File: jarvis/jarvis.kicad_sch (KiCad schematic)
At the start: 37 parts, among them IC1 ESP32-S3R16V, IC2 MAX98357AETE+T, IC3 MCP73871T-4CAI_ML, IC4 TLV70033DDCT, J1 Conn_01x02 - Speaker, J2 Mic Conn_01x05, J3 Conn_01x02 - Battery, U1 W25Q64JVSSIQ, U2 2137160001, Y1 Crystal 32.768khz, Y2 Crystal 40mhz

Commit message: flash routed
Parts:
- removed C1, C4, C5: 1uf, Capacitor_SMD:C_0603_1608Metric, symbol Device:C
- removed C10, C7, C8, C9: 12pf, Capacitor_SMD:C_0402_1005Metric, symbol Device:C
- removed C11, C12, C13, C14, C15, C16, C17: 0.1uf, Capacitor_SMD:C_0603_1608Metric, symbol Device:C
- removed C2, C6: 10uf, Capacitor_SMD:C_0603_1608Metric, symbol Device:C
- removed C3: 4.7uf, Capacitor_SMD:C_0603_1608Metric, symbol Device:C
- removed IC1: ESP32-S3R16V, jarvis:esp32-s3r16v, symbol jarvis:ESP32-S3R16V
- removed IC2: MAX98357AETE+T, jarvis:LIB_MAX98357AETE+T, symbol jarvis:MAX98357AETE+T
- removed IC3: MCP73871T-4CAI_ML, jarvis:MCP73871T-4CAI ML, symbol jarvis:MCP73871T-4CAI_ML
- removed IC4: TLV70033DDCT, jarvis:TLV70033DDCT, symbol jarvis:TLV70033DDCT
- removed J1: Conn_01x02 - Speaker, Connector_Molex:Molex_PicoBlade_53047-0210_1x02_P1.25mm_Vertical, symbol Connector_Generic:Conn_01x02
- removed J2: Mic Conn_01x05, Connector_Molex:Molex_PicoBlade_53047-0510_1x05_P1.25mm_Vertical, symbol Connector_Generic:Conn_01x05
- removed J3: Conn_01x02 - Battery, Connector_Molex:Molex_PicoBlade_53047-0210_1x02_P1.25mm_Vertical, symbol Connector_Generic:Conn_01x02
- removed L1: 24nh, jarvis:MLG1005SR24JT000, symbol jarvis:MLG1005SR24JT000
- removed PESD5: PESD5V0X1UAB,115, jarvis:PESD5V0X1UAB115, symbol jarvis:PESD5V0X1UAB,115
- removed R1: 2k, Resistor_SMD:R_0603_1608Metric, symbol Device:R
- removed R2: 10k, Resistor_SMD:R_0603_1608Metric, symbol Device:R
- removed R3, R4: 5.1k, Resistor_SMD:R_0603_1608Metric, symbol Device:R
- removed R5, R6: 22, Resistor_SMD:R_0603_1608Metric, symbol Device:R
- removed R7: 5M, Resistor_SMD:R_0603_1608Metric, symbol Device:R
- removed U1: W25Q64JVSSIQ, jarvis:W25Q64JVSSIQ, symbol jarvis:W25Q64JVSSIQ
- removed U2: 2137160001, jarvis:2137160001_MOL, symbol jarvis:2137160001
- removed Y1: Crystal 32.768khz, jarvis:XTAL_CM8V-T1A-32.768KHZ-7PF-20PPM-TA-QC, symbol jarvis:CM8V-T1A-32.768KHZ-7PF-20PPM-TA-QC
- removed Y2: Crystal 40mhz, jarvis:XTAL_CM8V-T1A-32.768KHZ-7PF-20PPM-TA-QC, symbol jarvis:CM8V-T1A-32.768KHZ-7PF-20PPM-TA-QC
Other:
- added sheet Components (components.kicad_sch)
- added sheet ESP (esp.kicad_sch)
- added sheet Power (untitled.kicad_sch)

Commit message: initial all connections
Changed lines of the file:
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@@
 			)
 		)
-		(pin "USB-DP" input
+		(pin "USB-DP" output
 			(at 213.36 52.07 180)
 			(effects

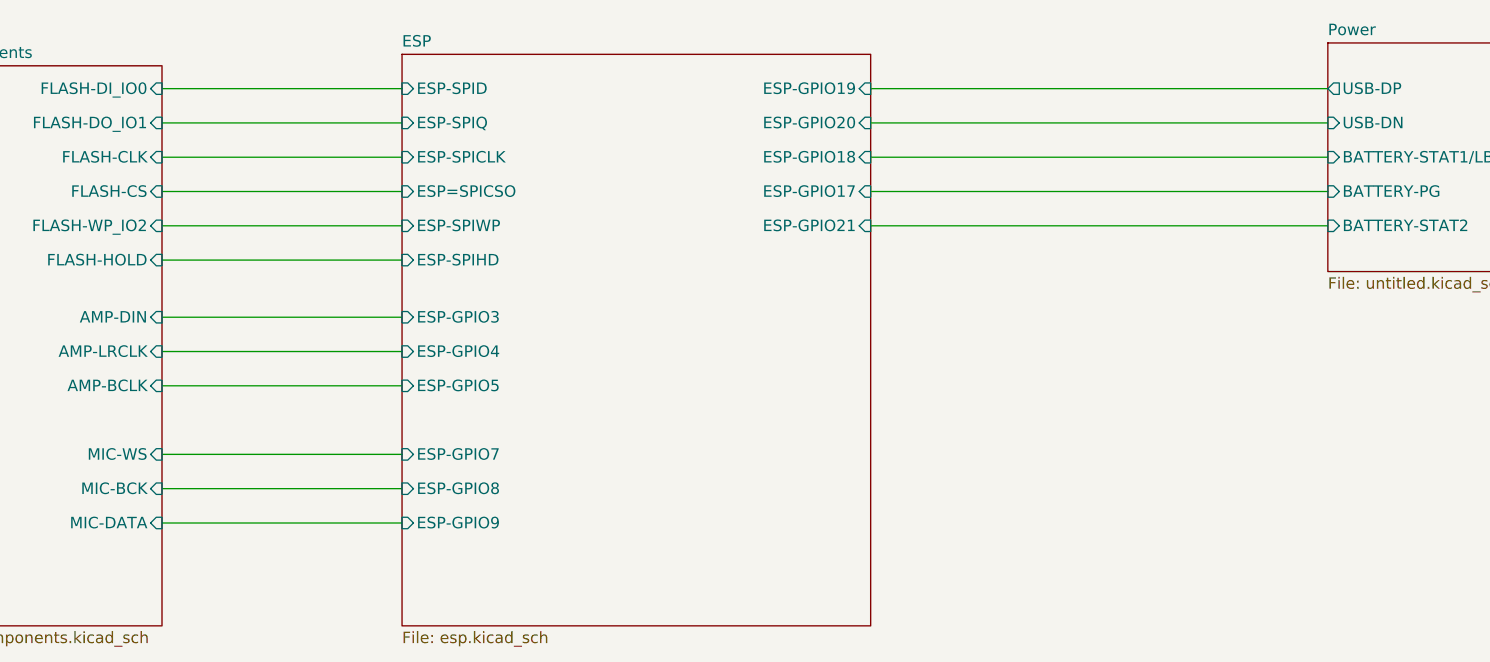
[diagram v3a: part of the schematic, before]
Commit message: with leds and boot button
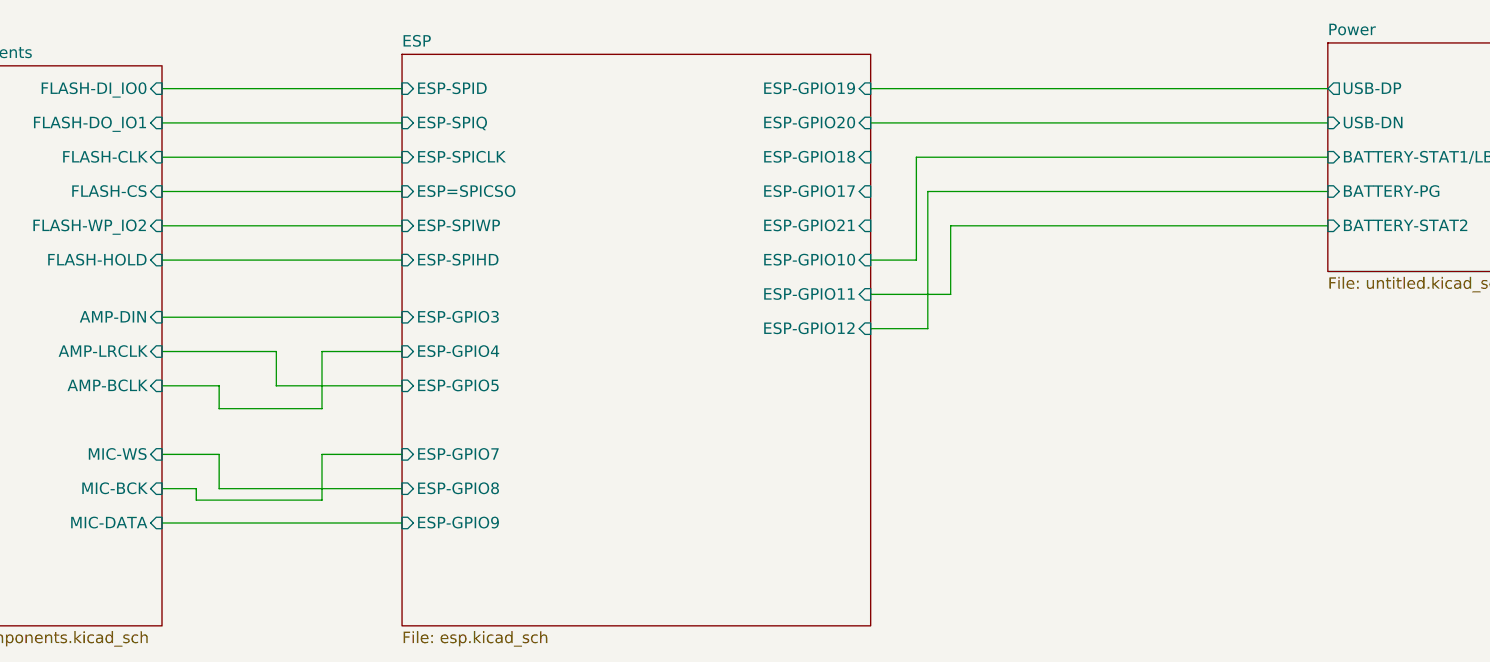
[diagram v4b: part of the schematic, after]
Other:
- sheet ESP ports: added ESP-GPIO10, ESP-GPIO11, ESP-GPIO12; removed none
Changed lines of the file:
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@@
 	(wire
 		(pts
-			(xy 83.82 81.28) (xy 110.49 81.28)
+			(xy 96.52 85.09) (xy 110.49 85.09)
 		)
 		(stroke
@@
 	(wire
 		(pts
+			(xy 87.63 97.79) (xy 87.63 96.52)
+		)
+		(stroke
+			(width 0)
+			(type default)
+		)
+	)
+	(wire
+		(pts
+			(xy 171.45 67.31) (xy 171.45 74.93)
+		)
+		(stroke
+			(width 0)
+			(type default)
+		)
+	)
+	(wire
+		(pts
 			(xy 83.82 100.33) (xy 110.49 100.33)
 		)
@@
 	(wire
 		(pts
-			(xy 83.82 96.52) (xy 110.49 96.52)
-		)
-		(stroke
-			(width 0)
-			(type default)
-		)
-	)
-	(wire
-		(pts
 			(xy 83.82 63.5) (xy 110.49 63.5)
 		)
@@
 	(wire
 		(pts
-			(xy 162.56 67.31) (xy 213.36 67.31)
+			(xy 171.45 74.93) (xy 162.56 74.93)
+		)
+		(stroke
+			(width 0)
+			(type default)
+		)
+	)
+	(wire
+		(pts
+			(xy 83.82 92.71) (xy 90.17 92.71)
+		)
+		(stroke
+			(width 0)
+			(type default)
+		)
+	)
+	(wire
+		(pts
+			(xy 168.91 63.5) (xy 213.36 63.5)
+		)
+		(stroke
+			(width 0)
+			(type default)
+		)
+	)
+	(wire
+		(pts
+			(xy 90.17 87.63) (xy 90.17 85.09)
+		)
+		(stroke
+			(width 0)
+			(type default)
+		)
+	)
+	(wire
+		(pts
+			(xy 87.63 96.52) (xy 83.82 96.52)
+		)
+		(stroke
+			(width 0)
+			(type default)
+		)
+	)
+	(wire
+		(pts
+			(xy 110.49 81.28) (xy 101.6 81.28)
+		)
+		(stroke
+			(width 0)
+			(type default)
+		)
+	)
+	(wire
+		(pts
+			(xy 96.52 81.28) (xy 96.52 85.09)
+		)
+		(stroke
+			(width 0)
+			(type default)
+		)
+	)
+	(wire
+		(pts
+			(xy 168.91 63.5) (xy 168.91 78.74)
 		)
 		(stroke
@@
 	(wire
 		(pts
-			(xy 83.82 85.09) (xy 110.49 85.09)
-		)
-		(stroke
-			(width 0)
-			(type default)
-		)
-	)
-	(wire
-		(pts
-			(xy 213.36 59.69) (xy 162.56 59.69)
+			(xy 83.82 81.28) (xy 96.52 81.28)
+		)
+		(stroke
+			(width 0)
+			(type default)
+		)
+	)
+	(wire
+		(pts
+			(xy 101.6 92.71) (xy 101.6 97.79)
+		)
+		(stroke
+			(width 0)
+			(type default)
+		)
+	)
+	(wire
+		(pts
+			(xy 167.64 71.12) (xy 167.64 59.69)
+		)
+		(stroke
+			(width 0)
+			(type default)
+		)
+	)
+	(wire
+		(pts
+			(xy 90.17 96.52) (xy 110.49 96.52)
+		)
+		(stroke
+			(width 0)
+			(type default)
+		)
+	)
+	(wire
+		(pts
+			(xy 101.6 97.79) (xy 87.63 97.79)
+		)
+		(stroke
+			(width 0)
+			(type default)
+		)
+	)
+	(wire
+		(pts
+			(xy 167.64 71.12) (xy 162.56 71.12)
+		)
+		(stroke
+			(width 0)
+			(type default)
+		)
+	)
+	(wire
+		(pts
+			(xy 90.17 92.71) (xy 90.17 96.52)
+		)
+		(stroke
+			(width 0)
+			(type default)
+		)
+	)
+	(wire
+		(pts
+			(xy 213.36 67.31) (xy 171.45 67.31)
+		)
+		(stroke
+			(width 0)
+			(type default)
+		)
+	)
+	(wire
+		(pts
+			(xy 83.82 85.09) (xy 90.17 85.09)
+		)
+		(stroke
+			(width 0)
+			(type default)
+		)
+	)
+	(wire
+		(pts
+			(xy 110.49 92.71) (xy 101.6 92.71)
+		)
+		(stroke
+			(width 0)
+			(type default)
+		)
+	)
+	(wire
+		(pts
+			(xy 101.6 87.63) (xy 90.17 87.63)
 		)
 		(stroke
@@
 	(wire
 		(pts
+			(xy 101.6 81.28) (xy 101.6 87.63)
+		)
+		(stroke
+			(width 0)
+			(type default)
+		)
+	)
+	(wire
+		(pts
+			(xy 167.64 59.69) (xy 213.36 59.69)
+		)
+		(stroke
+			(width 0)
+			(type default)
+		)
+	)
+	(wire
+		(pts
 			(xy 83.82 55.88) (xy 110.49 55.88)
 		)
@@
 	(wire
 		(pts
-			(xy 162.56 63.5) (xy 213.36 63.5)
+			(xy 162.56 78.74) (xy 168.91 78.74)
 		)
 		(stroke
@@
 		(pts
 			(xy 83.82 67.31) (xy 110.49 67.31)
-		)
-		(stroke
-			(width 0)
-			(type default)
-		)
-	)
-	(wire
-		(pts
-			(xy 83.82 92.71) (xy 110.49 92.71)
 		)
 		(stroke
@@
 			)
 		)
+		(pin "ESP-GPIO10" input
+			(at 162.56 71.12 0)
+			(effects
+				(font
+					(size 1.27 1.27)
+				)
+				(justify right)
+			)
+		)
+		(pin "ESP-GPIO11" input
+			(at 162.56 74.93 0)
+			(effects
+				(font
+					(size 1.27 1.27)
+				)
+				(justify right)
+			)
+		)
+		(pin "ESP-GPIO12" input
+			(at 162.56 78.74 0)
+			(effects
+				(font
+					(size 1.27 1.27)
+				)
+				(justify right)
+			)
+		)

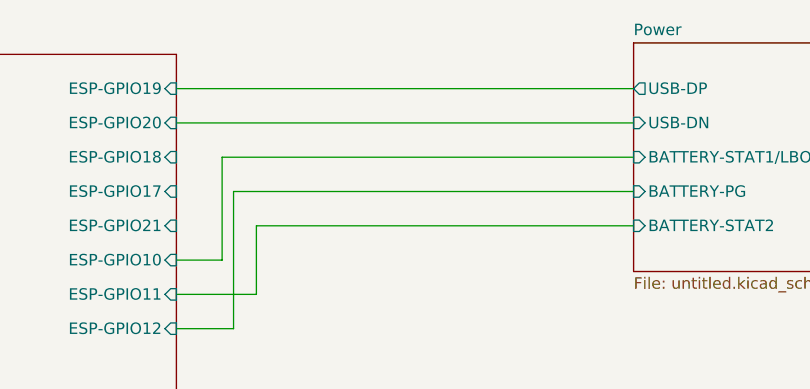
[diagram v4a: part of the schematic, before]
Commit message: small fixes from testing new pcb swap d lines connected pins on power ic that needed to be changed rbg led to be common anode
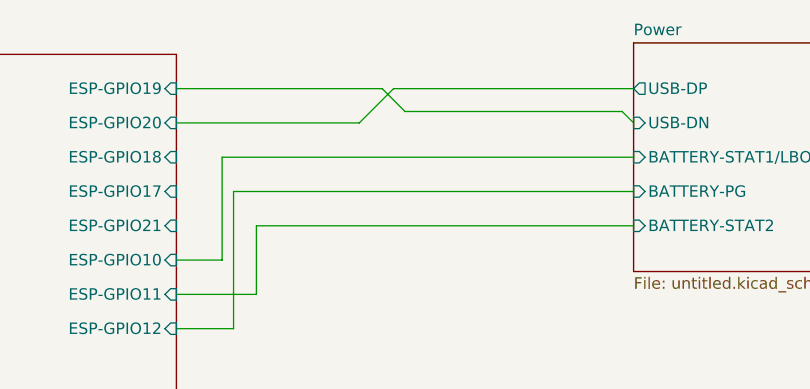
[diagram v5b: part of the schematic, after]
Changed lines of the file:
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@@
-	(wire
-		(pts
-			(xy 162.56 55.88) (xy 213.36 55.88)
-		)
-		(stroke
-			(width 0)
-			(type default)
-		)
-	)
 	(wire
 		(pts
@@
 	(wire
 		(pts
+			(xy 187.96 54.61) (xy 212.09 54.61)
+		)
+		(stroke
+			(width 0)
+			(type default)
+		)
+	)
+	(wire
+		(pts
 			(xy 83.82 59.69) (xy 110.49 59.69)
 		)
@@
 	(wire
 		(pts
+			(xy 186.69 52.07) (xy 182.88 55.88)
+		)
+		(stroke
+			(width 0)
+			(type default)
+		)
+	)
+	(wire
+		(pts
 			(xy 90.17 87.63) (xy 90.17 85.09)
 		)
@@
 	(wire
 		(pts
+			(xy 162.56 55.88) (xy 182.88 55.88)
+		)
+		(stroke
+			(width 0)
+			(type default)
+		)
+	)
+	(wire
+		(pts
 			(xy 110.49 81.28) (xy 101.6 81.28)
 		)
@@
 	(wire
 		(pts
+			(xy 162.56 52.07) (xy 185.42 52.07)
+		)
+		(stroke
+			(width 0)
+			(type default)
+		)
+	)
+	(wire
+		(pts
 			(xy 83.82 81.28) (xy 96.52 81.28)
 		)
@@
 	(wire
 		(pts
+			(xy 213.36 52.07) (xy 186.69 52.07)
+		)
+		(stroke
+			(width 0)
+			(type default)
+		)
+	)
+	(wire
+		(pts
+			(xy 212.09 54.61) (xy 213.36 55.88)
+		)
+		(stroke
+			(width 0)
+			(type default)
+		)
+	)
+	(wire
+		(pts
 			(xy 101.6 97.79) (xy 87.63 97.79)
 		)
@@
 	(wire
 		(pts
-			(xy 162.56 52.07) (xy 213.36 52.07)
-		)
-		(stroke
-			(width 0)
-			(type default)
-		)
-	)
-	(wire
-		(pts
 			(xy 83.82 77.47) (xy 110.49 77.47)
 		)
@@
 		)
 		(stroke
+			(width 0)
+			(type default)
+		)
+	)
+	(wire
+		(pts
+			(xy 185.42 52.07) (xy 187.96 54.61)
+		)
+		(stroke
